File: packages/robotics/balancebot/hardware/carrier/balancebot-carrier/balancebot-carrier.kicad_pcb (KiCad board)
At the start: 2 copper layers, 90 x 62 mm, 22 parts, among them J1 JST-XH pack in, J2 LM2596 module, J3 GY-521 MPU6050, J4 Motor left, J5 Motor right, Q1 ZXMP4A16G, U1 XIAO RP2350

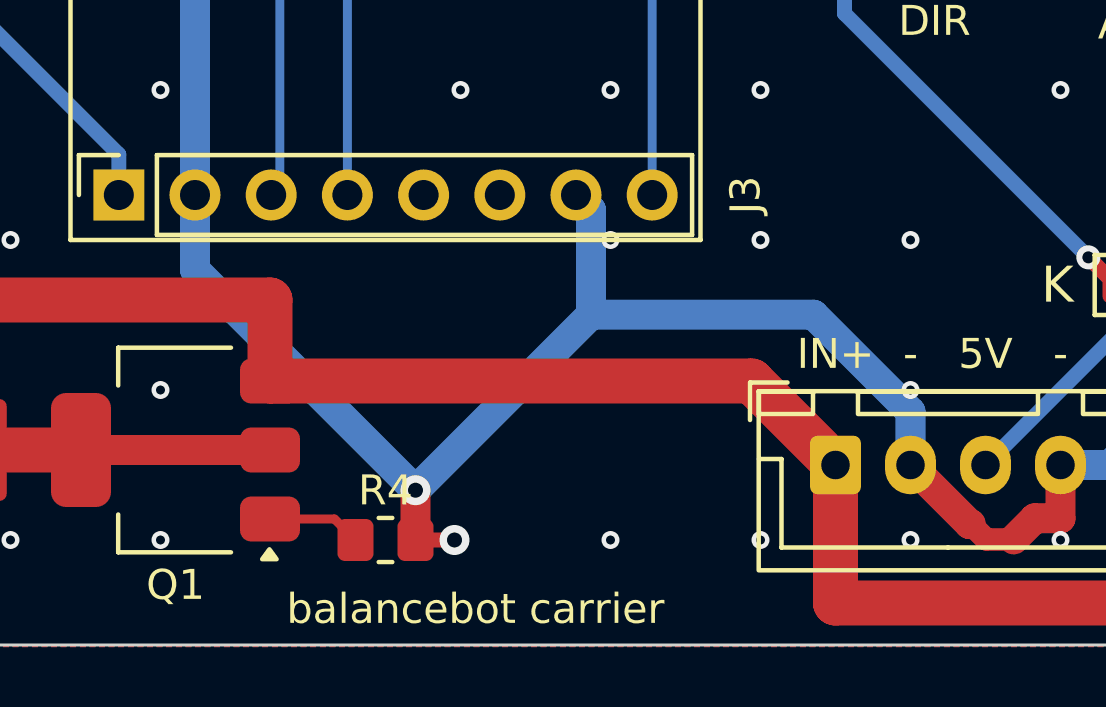
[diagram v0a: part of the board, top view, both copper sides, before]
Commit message: fix(balancebot): clamp Q1's gate with a 15 V zener
The pack-input text justified F1's 24 V rating by a hot-plug overshoot
above the 12.6 V pack, yet ruled out a gate zener because |VGS| reaches
only 12.6 V. The same overshoot lands on Q1's source while R4 holds the
gate at GND, so above 20 V it exceeds the ZXMP4A16G's VGSS (DS33584).

D2, a BZT52C15 (VZ 13.8-15.6 V at 5 mA, JSCJ Rev. 2.1), goes from Q1's
source (cathode) to its gate (anode); R4 limits its current. Its minimum
is above a full pack, so in use |VGS| still follows the pack (8.2-12.6 V,
past the -4.5 V the 100 mohm RDS(on) maximum is rated at), and in an
overshoot it holds |VGS| at or under 15.6 V (about 16.9 V at 125 C).

On the board D2 sits east of Q1's pins with all of PFET_GATE and its
cathode tie as fixed tracks: with only the anode tie fixed, its keepout
boxed in R4's gate pad and Freerouting left PFET_GATE unrouted on every
run. R4 moves down 0.5 mm and its reference beside it. The perfboard
gains a 1N4744A above Q1.

The README now gives a labelled hot-plug inrush estimate (about 30 A
peak, 80 us, above ISM's 21 A for about 30 us, no limiter), and the
Q1-to-A2 VBAT length as measured: 130.8 mm of track centreline; the
earlier 129 mm came from a path sum that skipped a 1.3 mm corner.

Co-Authored-By: Claude Opus 5.5 <noreply@anthropic.com>
Claude-Session: https://claude.ai/code/session_01DgeoMcrSCUfJwedu77q6oo
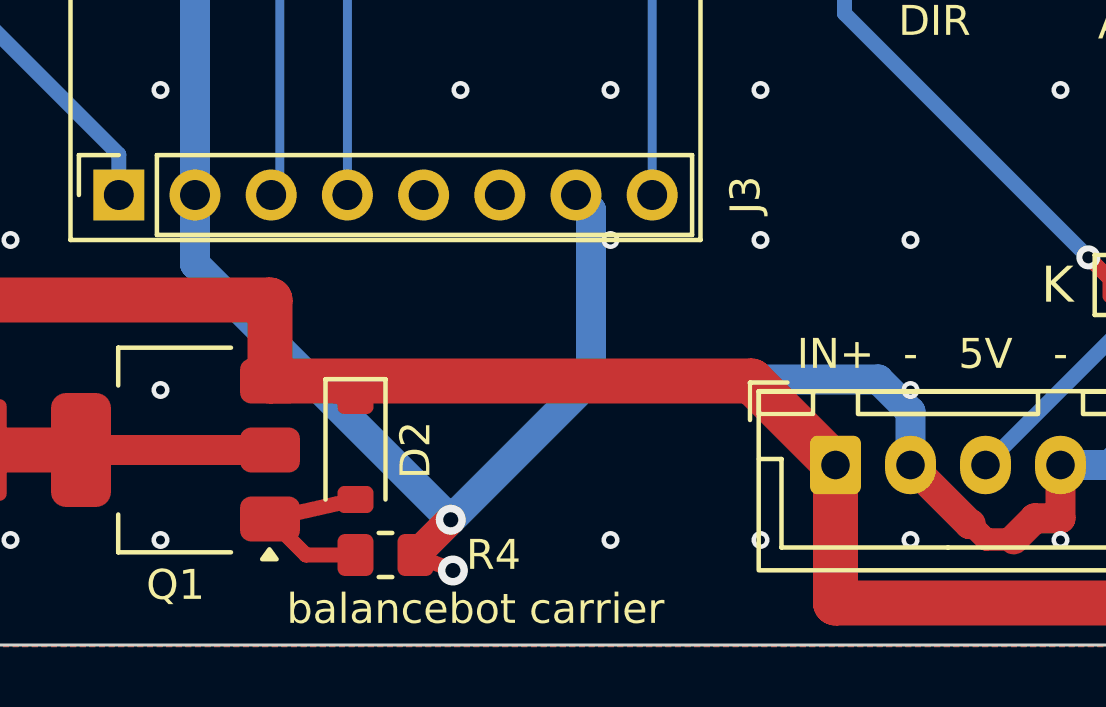
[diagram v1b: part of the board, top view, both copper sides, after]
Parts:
- added D2: BZT52C15, Diode_SMD:D_SOD-123, F.Cu at (144.0, 155.5)
- moved R4 0.50 mm to (145.0, 159.0)
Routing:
- net PFET_GATE: track 3.14 -> 6.27 mm
- net VBAT: track 204.2 -> 207.1 mm
- net GND: track 262.9 -> 264.0 mm
